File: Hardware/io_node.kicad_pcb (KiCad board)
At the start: 2 copper layers, 60 x 90 mm, 135 parts, among them J1 Conn_01x09, J10 Conn_01x04, J2 Conn_01x09, J3 Conn_01x09, J4 Conn_01x05, J5 USB_B_Micro, J6 Conn_01x05, J7 Conn_01x05, J8 Conn_01x02, J9 Conn_01x04, Q1 2N7002, Q2 2N7002, Q3 2N7002, Q4 2N7002, Q5 2N7002, Q6 2N7002, Q7 2N7002, Q8 2N7002, U1 STM32F103RBT6, U10 EL357N-G, U11 EL357N-G, U12 EL357N-G, U13 EL357N-G, U14 EL357N-G, U15 USBLC6-2SC6, U2 AMS1117-5.0, U3 AMS1117-3.3, U4 SP3485EN, U5 TLV274CPWR, U6 TLV274CPWR, U7 EL357N-G, U8 EL357N-G, U9 EL357N-G, Y1 8 MHz

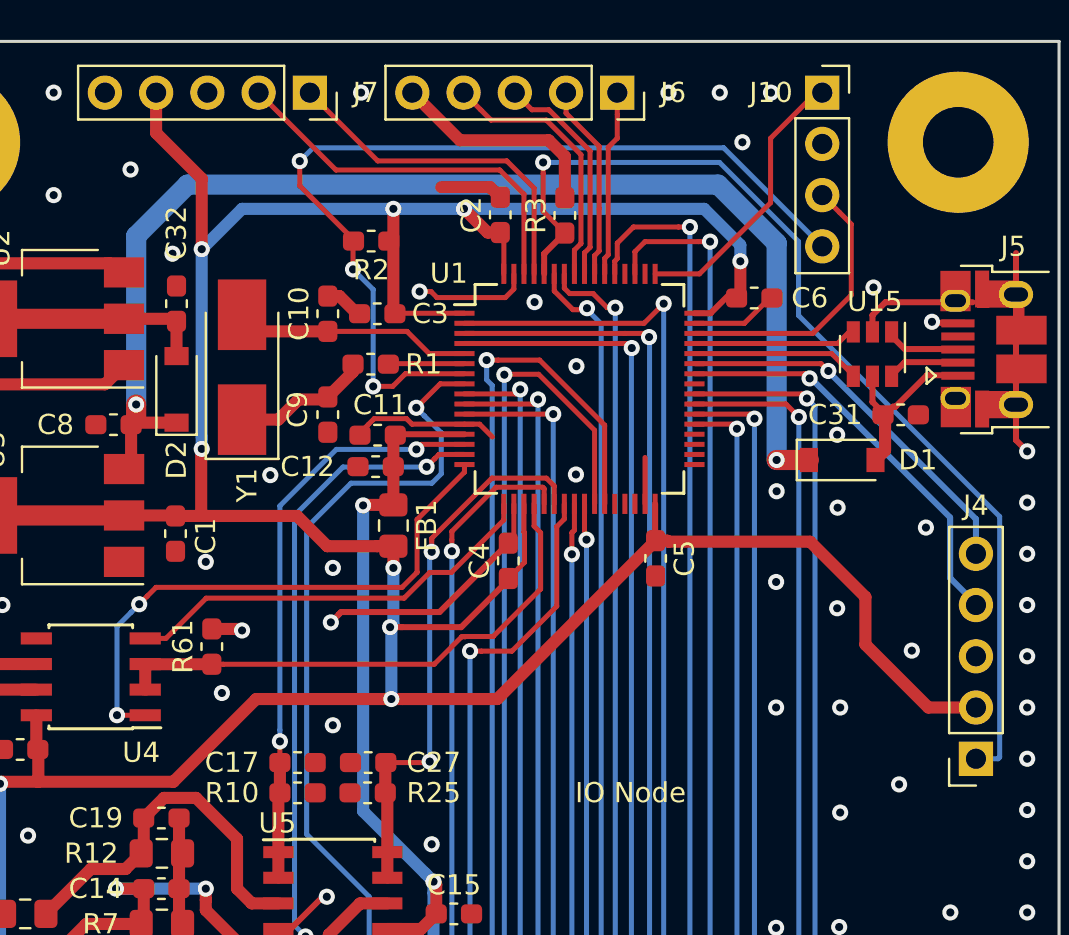
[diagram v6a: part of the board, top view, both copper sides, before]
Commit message: Adjust BOM for Node with divider
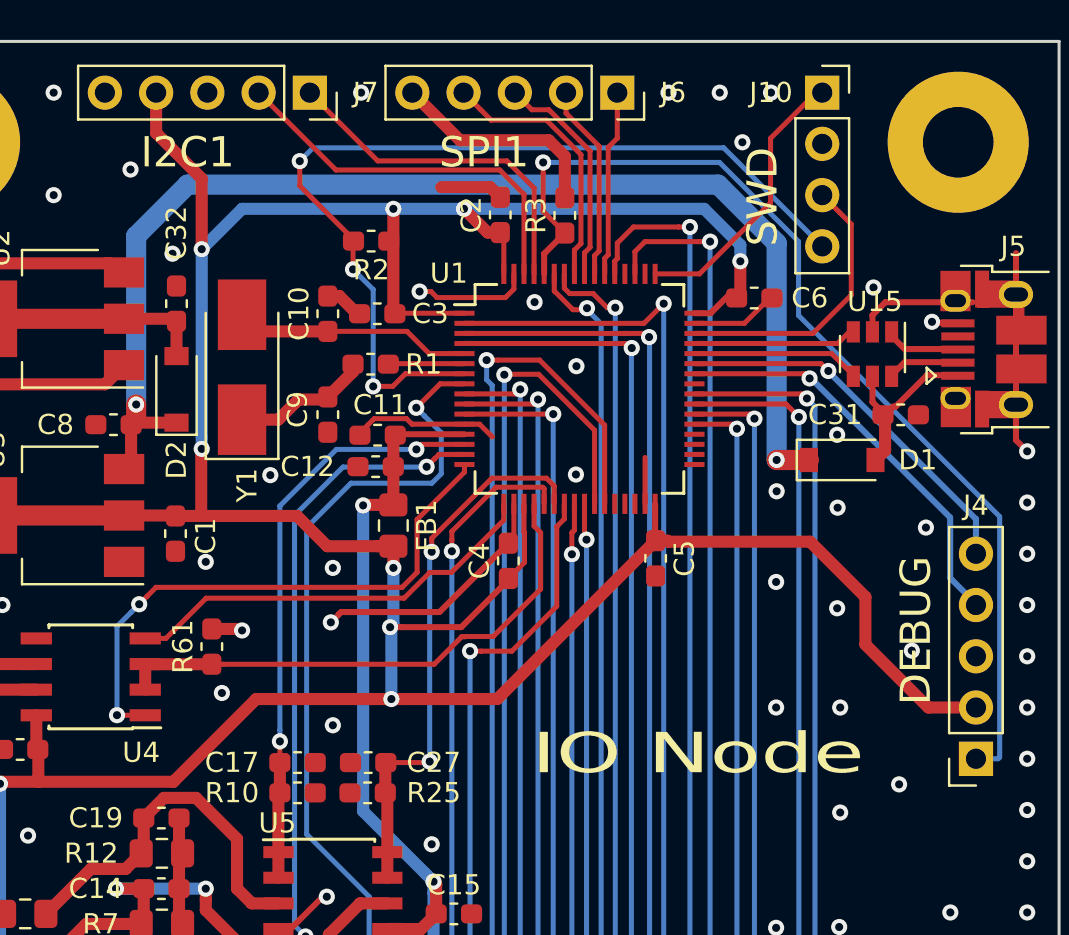
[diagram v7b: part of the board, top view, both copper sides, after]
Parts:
- R14, R17, R18, R23, R24, R5, R8, R9: value 150K -> 10K
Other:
- board text added: "3V3"
- board text added: "AIN_0"
- board text added: "AIN_1"
- board text added: "AIN_2"
- board text added: "AIN_3"
- board text added: "AIN_4"
- board text added: "AIN_5"
- board text added: "AIN_6"
- board text added: "AIN_7"
- board text added: "BOOT0"
- board text added: "CS"
- board text added: "DEBUG"
- board text added: "DIN_0"
- board text added: "DIN_1"
- board text added: "DIN_2"
- board text added: "DIN_3"
- board text added: "DIN_4"
- board text added: "DIN_5"
- board text added: "DIN_6"
- board text added: "DIN_7"
- board text added: "DOT_0"
- board text added: "DOT_1"
- board text added: "DOT_2"
- board text added: "DOT_3"
- board text added: "DOT_4"
- board text added: "DOT_5"
- board text added: "DOT_6"
- board text added: "DOT_7"
- board text added: "GND"
- board text added: "I2C1"
- board text added: "MISO"
- board text added: "MOSI"
- board text added: "NRST"
- board text added: "RS485_A"
- board text added: "RS485_B"
- board text added: "RX"
- board text added: "SCK"
- board text added: "SCL"
- board text added: "SDA"
- board text added: "SPI1"
- board text added: "SWCLK"
- board text added: "SWD"
- board text added: "SWDIO"
- board text added: "TX"
- board text added: "VIN"
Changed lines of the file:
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@@
-(kicad_pcb (version 20171130) (host pcbnew 5.1.5+dfsg1-2build2)
+(kicad_pcb (version 20171130) (host pcbnew "(5.0.1)-4")
   (general
     (thickness 1.6)
-    (drawings 9)
+    (drawings 64)
     (tracks 1105)
     (zones 0)
@@
   (layers
     (0 F.Cu signal)
-    (31 B.Cu signal hide)
+    (31 B.Cu signal)
     (32 B.Adhes user hide)
     (33 F.Adhes user hide)
     (34 B.Paste user hide)
     (35 F.Paste user hide)
-    (36 B.SilkS user hide)
+    (36 B.SilkS user)
     (37 F.SilkS user)
     (38 B.Mask user hide)
@@
     (zone_45_only no)
     (trace_min 0.2)
+    (segment_width 0.2)
+    (edge_width 0.15)
     (via_size 0.8)
     (via_drill 0.4)
@@
     (uvia_min_size 0.2)
     (uvia_min_drill 0.1)
-    (edge_width 0.15)
-    (segment_width 0.2)
     (pcb_text_width 0.3)
     (pcb_text_size 1.5 1.5)
@@
     (pad_to_mask_clearance 0.051)
     (solder_mask_min_width 0.25)
-    (aux_axis_origin 0 0)
+    (aux_axis_origin 45 105)
     (grid_origin 45 15)
     (visible_elements 7FFDFF7F)
@@
       (effects (font (size 1 1) (thickness 0.15)))
     )
-    (fp_text value 150K (at 0 1.65) (layer F.Fab)
+    (fp_text value 10K (at 0 1.65) (layer F.Fab)
       (effects (font (size 1 1) (thickness 0.15)))
     )
@@
       (effects (font (size 1 1) (thickness 0.15)))
     )
-    (fp_text value 150K (at 0 1.65) (layer F.Fab)
+    (fp_text value 10K (at 0 1.65) (layer F.Fab)
       (effects (font (size 1 1) (thickness 0.15)))
     )
@@
       (effects (font (size 1 1) (thickness 0.15)))
     )
-    (fp_text value 150K (at 0 1.65) (layer F.Fab)
+    (fp_text value 10K (at 0 1.65) (layer F.Fab)
       (effects (font (size 1 1) (thickness 0.15)))
     )
@@
       (effects (font (size 1 1) (thickness 0.15)))
     )
-    (fp_text value 150K (at 0 1.65) (layer F.Fab)
+    (fp_text value 10K (at 0 1.65) (layer F.Fab)
       (effects (font (size 1 1) (thickness 0.15)))
     )
@@
       (effects (font (size 1 1) (thickness 0.15)))
     )
-    (fp_text value 150K (at 0 1.65) (layer F.Fab)
+    (fp_text value 10K (at 0 1.65) (layer F.Fab)
       (effects (font (size 1 1) (thickness 0.15)))
     )
@@
       (effects (font (size 1 1) (thickness 0.15)))
     )
-    (fp_text value 150K (at 0 1.65) (layer F.Fab)
+    (fp_text value 10K (at 0 1.65) (layer F.Fab)
       (effects (font (size 1 1) (thickness 0.15)))
     )
@@
       (effects (font (size 1 1) (thickness 0.15)))
     )
-    (fp_text value 150K (at 0 1.65) (layer F.Fab)
+    (fp_text value 10K (at 0 1.65) (layer F.Fab)
       (effects (font (size 1 1) (thickness 0.15)))
     )
@@
       (effects (font (size 1 1) (thickness 0.15)))
     )
-    (fp_text value 150K (at 0 1.65) (layer F.Fab)
+    (fp_text value 10K (at 0 1.65) (layer F.Fab)
       (effects (font (size 1 1) (thickness 0.15)))
     )
@@
     )
   )
-  (gr_text "IO Node" (at 83.76 52.25) (layer F.SilkS)
-    (effects (font (size 1 1) (thickness 0.15)))
+  (gr_text NRST (at 89.1 25.3) (layer B.SilkS)
+    (effects (font (size 1.5 1.5) (thickness 0.3)) (justify mirror))
+  )
+  (gr_text SWDIO (at 88.4 22.7) (layer B.SilkS)
+    (effects (font (size 1.5 1.5) (thickness 0.3)) (justify mirror))
+  )
+  (gr_text GND (at 89.6 20.1) (layer B.SilkS)
+    (effects (font (size 1.5 1.5) (thickness 0.3)) (justify mirror))
+  )
+  (gr_text SWCLK (at 88.1 17.6) (layer B.SilkS)
+    (effects (font (size 1.5 1.5) (thickness 0.3)) (justify mirror))
+  )
+  (gr_text RX (at 97.8 40.6) (layer B.SilkS)
+    (effects (font (size 1.5 1.5) (thickness 0.3)) (justify mirror))
+  )
+  (gr_text TX (at 98 43) (layer B.SilkS)
+    (effects (font (size 1.5 1.5) (thickness 0.3)) (justify mirror))
+  )
+  (gr_text GND (at 97.5 45.6) (layer B.SilkS)
+    (effects (font (size 1.5 1.5) (thickness 0.3)) (justify mirror))
+  )
+  (gr_text 3V3 (at 97.5 48.2) (layer B.SilkS)
+    (effects (font (size 1.5 1.5) (thickness 0.3)) (justify mirror))
+  )
+  (gr_text BOOT0 (at 96.1 50.7) (layer B.SilkS)
+    (effects (font (size 1.5 1.5) (thickness 0.3)) (justify mirror))
+  )
+  (gr_text DOT_0 (at 96.3 66) (layer B.SilkS)
+    (effects (font (size 1.5 1.5) (thickness 0.3)) (justify mirror))
+  )
+  (gr_text DOT_1 (at 96.3 68.4) (layer B.SilkS)
+    (effects (font (size 1.5 1.5) (thickness 0.3)) (justify mirror))
+  )
+  (gr_text DOT_2 (at 96.3 70.9) (layer B.SilkS)
+    (effects (font (size 1.5 1.5) (thickness 0.3)) (justify mirror))
+  )
+  (gr_text DOT_3 (at 96.2 73.4) (layer B.SilkS)
+    (effects (font (size 1.5 1.5) (thickness 0.3)) (justify mirror))
+  )
+  (gr_text DOT_4 (at 96.2 75.9) (layer B.SilkS)
+    (effects (font (size 1.5 1.5) (thickness 0.3)) (justify mirror))
+  )
+  (gr_text DOT_5 (at 96.2 78.5) (layer B.SilkS)
+    (effects (font (size 1.5 1.5) (thickness 0.3)) (justify mirror))
+  )
+  (gr_text DOT_6 (at 96.2 81) (layer B.SilkS)
+    (effects (font (size 1.5 1.5) (thickness 0.3)) (justify mirror))
+  )
+  (gr_text DOT_7 (at 96.2 83.7) (layer B.SilkS)
+    (effects (font (size 1.5 1.5) (thickness 0.3)) (justify mirror))
+  )
+  (gr_text GND (at 97.3 86.3) (layer B.SilkS)
+    (effects (font (size 1.5 1.5) (thickness 0.3)) (justify mirror))
+  )
+  (gr_text DIN_0 (at 65.6 96.4 90) (layer B.SilkS)
+    (effects (font (size 1.5 1.5) (thickness 0.3)) (justify mirror))
+  )
+  (gr_text DIN_1 (at 68 96.4 90) (layer B.SilkS)
+    (effects (font (size 1.5 1.5) (thickness 0.3)) (justify mirror))
+  )
+  (gr_text DIN_2 (at 70.4 96.4 90) (layer B.SilkS)
+    (effects (font (size 1.5 1.5) (thickness 0.3)) (justify mirror))
+  )
+  (gr_text DIN_3 (at 72.9 96.4 90) (layer B.SilkS)
+    (effects (font (size 1.5 1.5) (thickness 0.3)) (justify mirror))
+  )
+  (gr_text DIN_4 (at 75.5 96.4 90) (layer B.SilkS)
+    (effects (font (size 1.5 1.5) (thickness 0.3)) (justify mirror))
+  )
+  (gr_text DIN_5 (at 78.2 96.4 90) (layer B.SilkS)
+    (effects (font (size 1.5 1.5) (thickness 0.3)) (justify mirror))
+  )
+  (gr_text DIN_6 (at 80.7 96.4 90) (layer B.SilkS)
+    (effects (font (size 1.5 1.5) (thickness 0.3)) (justify mirror))
+  )
+  (gr_text DIN_7 (at 83.2 96.4 90) (layer B.SilkS)
+    (effects (font (size 1.5 1.5) (thickness 0.3)) (justify mirror))
+  )
+  (gr_text GND (at 85.7 97.1 90) (layer B.SilkS)
+    (effects (font (size 1.5 1.5) (thickness 0.3)) (justify mirror))
+  )
+  (gr_text GND (at 51.8 78.7) (layer B.SilkS)
+    (effects (font (size 1.5 1.5) (thickness 0.3)) (justify mirror))
+  )
+  (gr_text AIN_7 (at 52.7 76.1) (layer B.SilkS)
+    (effects (font (size 1.5 1.5) (thickness 0.3)) (justify mirror))
+  )
+  (gr_text AIN_6 (at 52.7 73.5) (layer B.SilkS)
+    (effects (font (size 1.5 1.5) (thickness 0.3)) (justify mirror))
+  )
+  (gr_text AIN_5 (at 52.7 70.9) (layer B.SilkS)
+    (effects (font (size 1.5 1.5) (thickness 0.3)) (justify mirror))
+  )
+  (gr_text AIN_4 (at 52.7 68.4) (layer B.SilkS)
+    (effects (font (size 1.5 1.5) (thickness 0.3)) (justify mirror))
+  )
+  (gr_text AIN_3 (at 52.7 65.9) (layer B.SilkS)
+    (effects (font (size 1.5 1.5) (thickness 0.3)) (justify mirror))
+  )
+  (gr_text AIN_2 (at 52.7 63.2) (layer B.SilkS)
+    (effects (font (size 1.5 1.5) (thickness 0.3)) (justify mirror))
+  )
+  (gr_text AIN_1 (at 52.7 60.7) (layer B.SilkS)
+    (effects (font (size 1.5 1.5) (thickness 0.3)) (justify mirror))
+  )
+  (gr_text AIN_0 (at 52.7 58.2) (layer B.SilkS)
+    (effects (font (size 1.5 1.5) (thickness 0.3)) (justify mirror))
+  )
+  (gr_text GND (at 51.7 50.9) (layer B.SilkS)
+    (effects (font (size 1.5 1.5) (thickness 0.3)) (justify mirror))
+  )
+  (gr_text RS485_B (at 54.4 48.1) (layer B.SilkS)
+    (effects (font (size 1.5 1.5) (thickness 0.3)) (justify mirror))
+  )
+  (gr_text RS485_A (at 54.5 45.6) (layer B.SilkS)
+    (effects (font (size 1.5 1.5) (thickness 0.3)) (justify mirror))
+  )
+  (gr_text VIN (at 51.4 43) (layer B.SilkS)
+    (effects (font (size 1.5 1.5) (thickness 0.3)) (justify mirror))
+  )
+  (gr_text GND (at 51.7 30.3) (layer B.SilkS)
+    (effects (font (size 1.5 1.5) (thickness 0.3)) (justify mirror))
+  )
+  (gr_text VIN (at 51.3 27.8) (layer B.SilkS)
+    (effects (font (size 1.5 1.5) (thickness 0.3)) (justify mirror))
+  )
+  (gr_text CS (at 83.2 20.5 90) (layer B.SilkS)
+    (effects (font (size 1.5 1.5) (thickness 0.3)) (justify mirror))
+  )
+  (gr_text SCK (at 80.7 21.3 90) (layer B.SilkS)
+    (effects (font (size 1.5 1.5) (thickness 0.3)) (justify mirror))
+  )
+  (gr_text MISO (at 78.2 21.7 90) (layer B.SilkS)
+    (effects (font (size 1.5 1.5) (thickness 0.3)) (justify mirror))
+  )
+  (gr_text MOSI (at 75.7 21.7 90) (layer B.SilkS)
+    (effects (font (size 1.5 1.5) (thickness 0.3)) (justify mirror))
+  )
+  (gr_text GND (at 72.9 21.4 90) (layer B.SilkS)
+    (effects (font (size 1.5 1.5) (thickness 0.3)) (justify mirror))
+  )
+  (gr_text GND (at 57.7 21.3 90) (layer B.SilkS)
+    (effects (font (size 1.5 1.5) (thickness 0.3)) (justify mirror))
+  )
+  (gr_text 3V3 (at 60.4 21.3 90) (layer B.SilkS)
+    (effects (font (size 1.5 1.5) (thickness 0.3)) (justify mirror))
+  )
+  (gr_text SCL (at 67.9 21.3 90) (layer B.SilkS)
+    (effects (font (size 1.5 1.5) (thickness 0.3)) (justify mirror))
+  )
+  (gr_text SDA (at 65.3 21.3 90) (layer B.SilkS)
+    (effects (font (size 1.5 1.5) (thickness 0.3)) (justify mirror))
+  )
+  (gr_text DEBUG (at 97.9 44.2 90) (layer F.SilkS)
+    (effects (font (size 1.5 1.5) (thickness 0.3)))
+  )
+  (gr_text SWD (at 90.3 22.7 90) (layer F.SilkS)
+    (effects (font (size 1.5 1.5) (thickness 0.3)))
+  )
+  (gr_text SPI1 (at 76.5 20.5) (layer F.SilkS)
+    (effects (font (size 1.5 1.5) (thickness 0.3)))
+  )
+  (gr_text I2C1 (at 61.8 20.5) (layer F.SilkS)
+    (effects (font (size 1.5 1.5) (thickness 0.3)))
+  )
+  (gr_text "IO Node" (at 87.1 50.3) (layer F.SilkS)
+    (effects (font (size 2 3) (thickness 0.25)))
   )
   (dimension 90 (width 0.3) (layer F.Fab)
